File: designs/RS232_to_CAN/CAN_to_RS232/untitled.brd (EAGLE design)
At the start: 34 x 55 mm, 22 parts, among them IC1 UART_RS232, IC2 STM32F042K6T6TR, IC3 CAN_Receiver, J1 Programmer, J2 CAN, J3 RS232

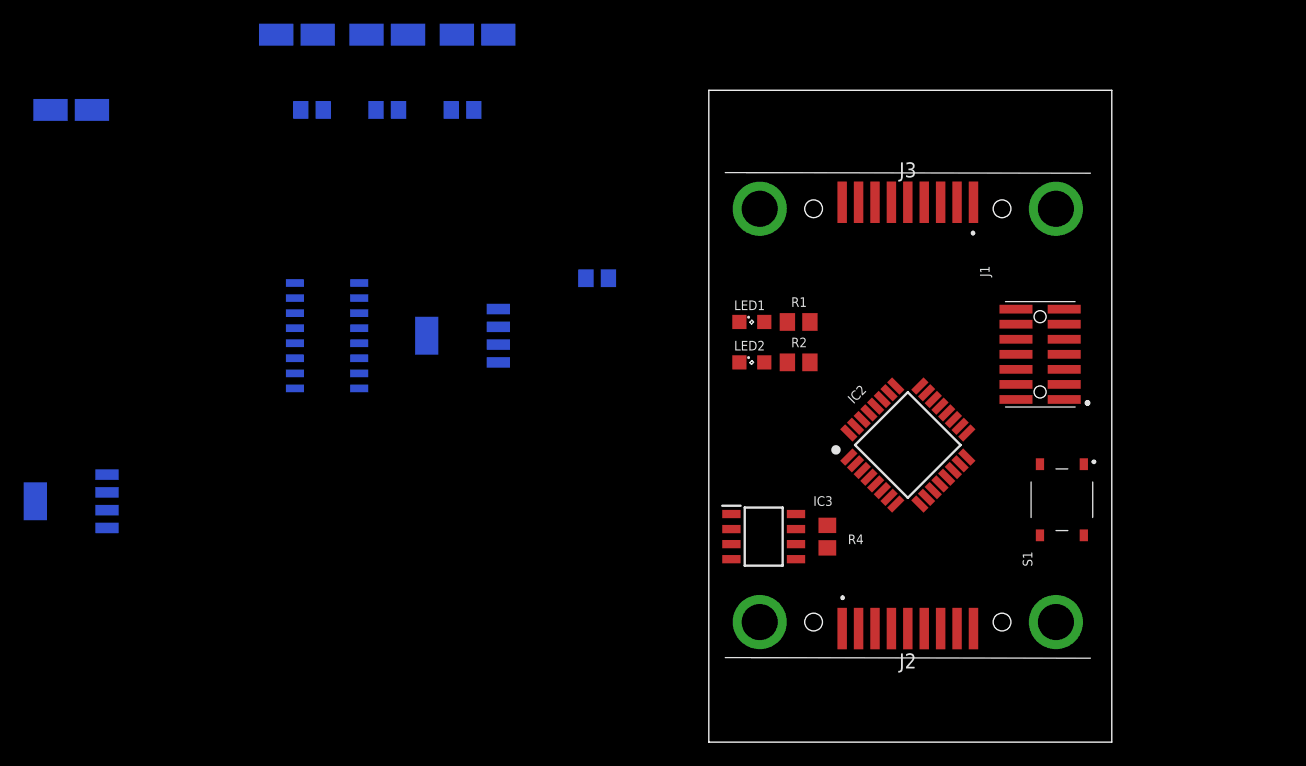
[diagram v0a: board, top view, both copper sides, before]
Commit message: ESP32 brd layout
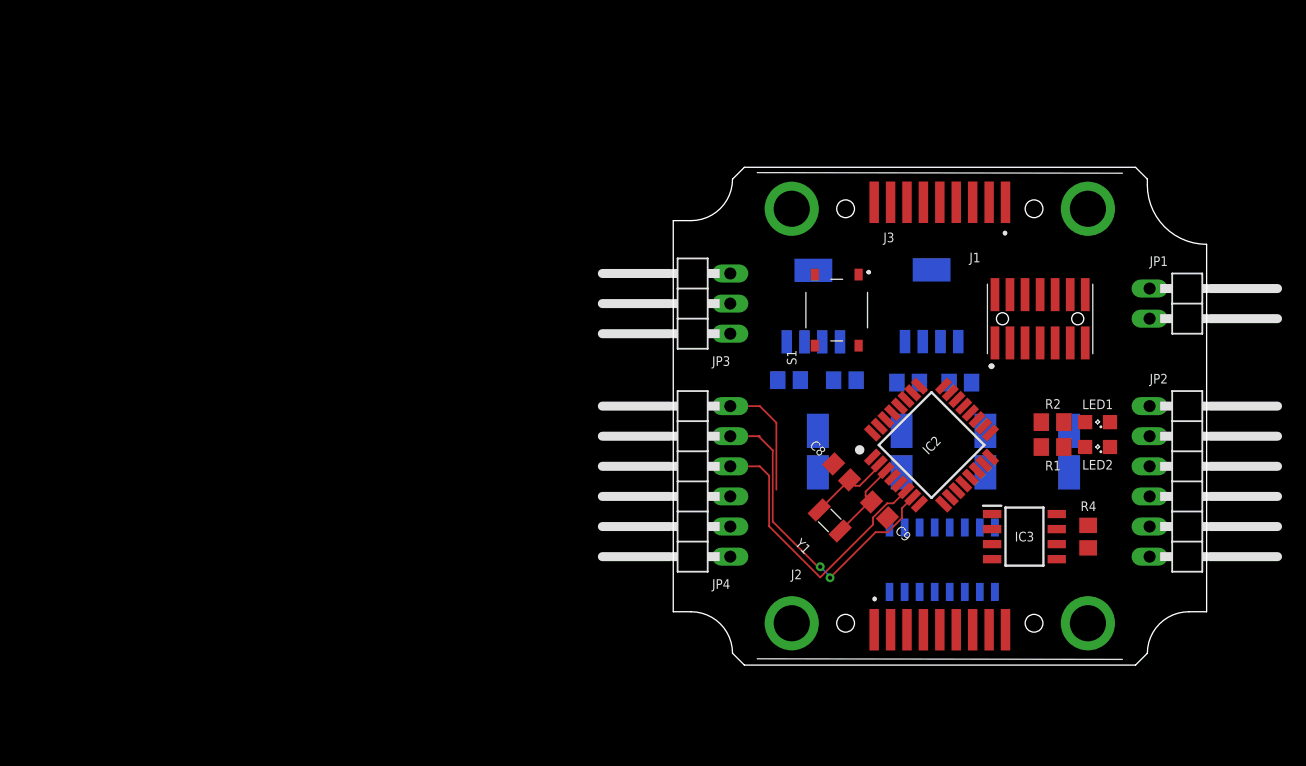
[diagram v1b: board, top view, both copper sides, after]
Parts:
- added C8, C9: 9pf, CommonParts:C0805
- added JP1: Power, pinhead:1X02/90
- added JP2: SPI, pinhead:1X06/90
- added JP3: I2C, pinhead:1X03/90
- added JP4: (no value), pinhead:1X06/90
- added Y1: OSC1, MouserUseful:CM7VT1A32768KHZ7PF100PPMTAQC
- moved C1 89.0 mm to (33.4, 24.5), turned to 270 degrees
- moved PS1 74.5 mm to (21.8, 36.8), turned to 90 degrees
- moved C7 59.3 mm to (24.2, 30.3)
- moved C4 56.3 mm to (12.2, 24.5), turned to 270 degrees
- moved C3 55.9 mm to (19.3, 24.5), turned to 270 degrees
- moved C2 55.4 mm to (26.3, 24.5), turned to 270 degrees
- moved IC1 55.2 mm to (22.7, 15.4), turned to 270 degrees
- moved C5 44.1 mm to (19.8, 30.3)
- moved C6 40.9 mm to (9.77, 30.5)
- moved LED1 30.4 mm to (35.8, 27.0), turned to 180 degrees
- moved LED2 30.0 mm to (35.8, 24.9), turned to 180 degrees
- moved PS2 29.7 mm to (11.8, 36.8), turned to 90 degrees
- moved S1 24.8 mm to (13.8, 36.5)
- moved R1 23.9 mm to (32.0, 24.9), turned to 180 degrees
- moved R3 22.6 mm to (14.5, 30.5)
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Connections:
- removed net N$4: IC2.15
- removed net N$5: C2.1
- removed net N$6: C2.2
- removed net N$7: C3.1
- removed net N$8: IC2.14
- new net CLK: IC2.11, JP2.2
- new net CS: IC2.10, JP2.3
- new net CS2: IC2.9, JP2.4
- new net MISO: IC2.12, JP2.5
- new net MOSI: IC2.13, JP2.6
- new net OSC_IN: C8.1, IC2.2, Y1.2
- new net OSC_OUT: C9.2, IC2.3, Y1.1
- new net PA0: IC2.6, JP4.4
- new net PA1: IC2.7, JP4.5
- new net PA2: IC2.8, JP4.6
- new net SCL: IC2.29, JP3.2
- new net SDA: IC2.30, JP3.3
- net 3.3V: now also JP4.1
- net 5V: now also JP4.2
- net 5V_IN: now also JP1.1
- net AGND: now also JP1.2, JP2.1, JP3.1, JP4.3
- net C1-: now also C3.1
- net C2+: now also C2.2
- net C2-: now also C2.1
- net GNDA: now also C8.2, C9.1
- net LED1: now also IC2.15
- net LED2: now also IC2.14
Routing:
- net PA1: track 0.00 -> 27.3 mm, vias 0 -> 2
- net PA0: track 0.00 -> 24.6 mm
- net PA2: track 0.00 -> 10.1 mm
- net OSC_OUT: track 0.00 -> 7.22 mm
- net OSC_IN: track 0.00 -> 7.21 mm
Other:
- board size 34 x 55 mm -> 45 x 42 mm

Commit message: added brd layout for RS232 to can
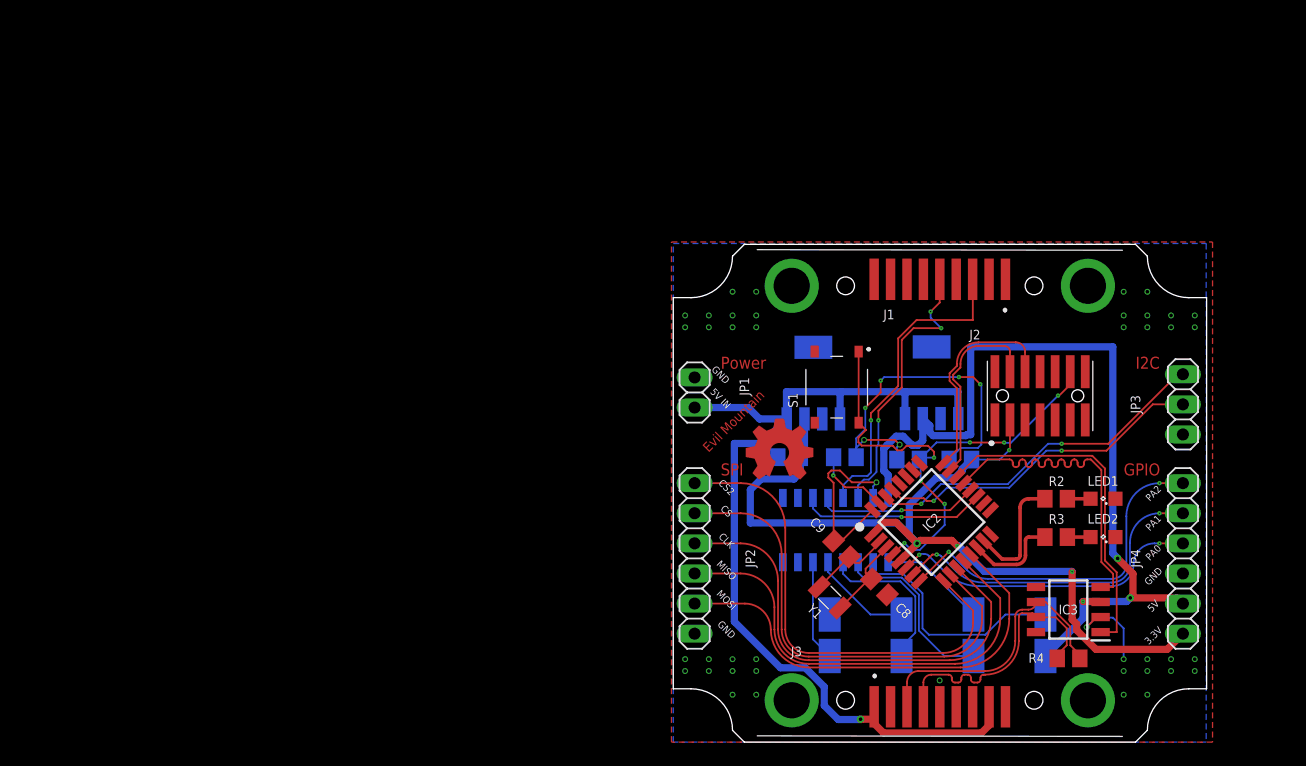
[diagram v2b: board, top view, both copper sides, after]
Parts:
- J1: value Programmer -> RS232; device MouserUseful:FTSH10701LDVKA -> MouserUseful:K202XHTE9SN
- J2: value CAN -> Programmer; device MouserUseful:K202XHTE9SN -> MouserUseful:FTSH10701LDVKA
- J3: value RS232 -> CAN
- JP1: value Power -> (none); device pinhead:1X02/90 -> pinhead:1X02
- JP2: value SPI -> (none); device pinhead:1X06/90 -> pinhead:1X06
- JP3: value I2C -> (none); device pinhead:1X03/90 -> pinhead:1X03
- JP4: device pinhead:1X06/90 -> pinhead:1X06
- R1: value 10Ohm -> 10kOhm
- R3: value 10kOhm -> 10Ohm
- moved J3 43.6 mm to (22.5, 2.48), turned to 180 degrees
- moved JP1 42.9 mm to (1.80, 29.5), turned to 90 degrees
- moved JP3 42.9 mm to (43.0, 28.5)
- moved JP2 42.7 mm to (1.80, 15.5), turned to 90 degrees
- moved JP4 42.5 mm to (43.0, 15.5)
- moved R3 22.2 mm to (32.3, 17.3), flipped to the top, turned to 180 degrees
- moved J2 21.9 mm to (30.9, 29.2), turned to 0 degrees
- moved C3 19.7 mm to (31.4, 9.02), turned to 90 degrees
- moved R1 17.5 mm to (14.5, 24.0), flipped to the bottom, turned to 0 degrees
- moved C1 17.5 mm to (25.3, 9.02), turned to 90 degrees
- moved C2 17.0 mm to (19.3, 9.02)
- moved C4 15.5 mm to (13.2, 9.02)
- moved R4 10.4 mm to (33.4, 7.07), turned to 180 degrees
- moved C8 10.2 mm to (17.4, 13.1)
- moved IC1 9.34 mm to (13.7, 17.9), turned to 90 degrees
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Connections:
- removed net AGND: IC1.15, IC3.2, IC3.8, J2.3, J2.6, J3.5, JP1.2, JP2.1, JP3.1, JP4.3
- removed net CAN_H: IC3.7, J2.7, R4.2
- removed net CAN_L: IC3.6, J2.2, R4.1
- removed net GNDA: C4.1, C5.2, C6.2, C7.2, C8.2, C9.1, IC2.16, IC2.32, J1.11, LED1.C, LED2.C, PS1.5, PS2.5, R3.1, S1.3, S1.4
- new net CAN_N: IC3.6, J3.2, R4.1
- new net CAN_P: IC3.7, J3.7, R4.2
- new net CAN_UC_XD_N: IC2.21, IC3.4
- new net CAN_UC_XD_P: IC2.22, IC3.1
- new net RXD_UC: IC1.12, IC2.20
- new net TXD_UC: IC1.11, IC2.19
- net 3.3V: now also J2.3
- net 5V: now also C3.1; no longer C1.1
- net 5V_IN: now also J3.1, J3.9; no longer J2.1, J2.9
- net C1+: now also C1.2; no longer C3.2
- net C1-: now also C1.1; no longer C3.1
- net CLK: now also JP2.4; no longer JP2.2
- net CS: now also JP2.5; no longer JP2.3
- net CS2: now also JP2.6; no longer JP2.4
- net GND: now also C4.1, C5.2, C6.2, C7.2, C8.1, C9.2, IC1.15, IC2.16, IC2.32, IC3.2, IC3.8, J2.11, J2.5, J2.7, J3.3, J3.6, JP1.2, JP2.1, JP3.1, JP4.3, LED1.C, LED2.C, PS1.5, PS2.5, R1.1, S1.3, S1.4; no longer J1.7
- net LED1: now also R2.2; no longer R1.2
- net LED2: now also R3.2; no longer R2.2
- net MISO: now also JP2.3; no longer JP2.5
- net MOSI: now also JP2.2; no longer JP2.6
- net N$1: now also R2.1; no longer R1.1
- net N$2: now also R3.1; no longer R2.1
- net N$3: now also R1.2; no longer R3.2
- net NRST: now also J2.12; no longer J1.12
- net OSC_IN: now also C9.1; no longer C8.1
- net OSC_OUT: now also C8.2; no longer C9.2
- net RXD: now also J1.2; no longer IC1.12, IC2.20, IC2.21, IC3.4, J3.2
- net SWCLK: now also J2.6; no longer J1.6
- net SWIDO: now also J2.4; no longer J1.4
- net SWO: now also J2.8; no longer J1.8
- net TXD: now also J1.3; no longer IC1.11, IC2.19, IC2.22, IC3.1, J3.3
- net VS+: now also C3.2; no longer C1.2
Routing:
- net 5V_IN: track 0.00 -> 82.7 mm, vias 0 -> 1
- net 3.3V: track 0.00 -> 80.4 mm, vias 0 -> 4
- net 5V: track 0.00 -> 73.0 mm, vias 0 -> 3
- net GND: track 0.00 -> 55.0 mm, vias 0 -> 49
- net NRST: track 0.00 -> 45.8 mm, vias 0 -> 7
- net CS2: track 0.00 -> 40.1 mm
- net CS: track 0.00 -> 39.2 mm
- net CLK: track 0.00 -> 38.5 mm
- net MISO: track 0.00 -> 37.8 mm
- net MOSI: track 0.00 -> 37.3 mm
- net SDA: track 0.00 -> 29.9 mm, vias 0 -> 2
- net CAN_UC_XD_P: track 0.00 -> 29.2 mm
- net SCL: track 0.00 -> 28.3 mm, vias 0 -> 2
- net CAN_UC_XD_N: track 0.00 -> 28.2 mm
- net RXD: track 0.00 -> 26.5 mm, vias 0 -> 1
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- added copper zone on layer 1, net GND
- added copper zone on layer 16, net GND
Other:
- outline, holes or cut-outs redrawn
- board text added: "3.3V"
- board text added: "5V"
- board text added: "5V IN"
- board text added: "CLK"
- board text added: "CS"
- board text added: "CS2"
- board text added: "Evil Mountain"
- board text added: "GND"
- board text added: "GPIO"
- board text added: "I2C"
- board text added: "MISO"
- board text added: "MOSI"
- board text added: "PA0"
- board text added: "PA1"
- board text added: "PA2"
- board text added: "Power"
- board text added: "SCL"
- board text added: "SDA"
- board text added: "SPI"
